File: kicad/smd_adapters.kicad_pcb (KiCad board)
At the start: 2 copper layers, 79.8 x 69.7 mm, 24 parts

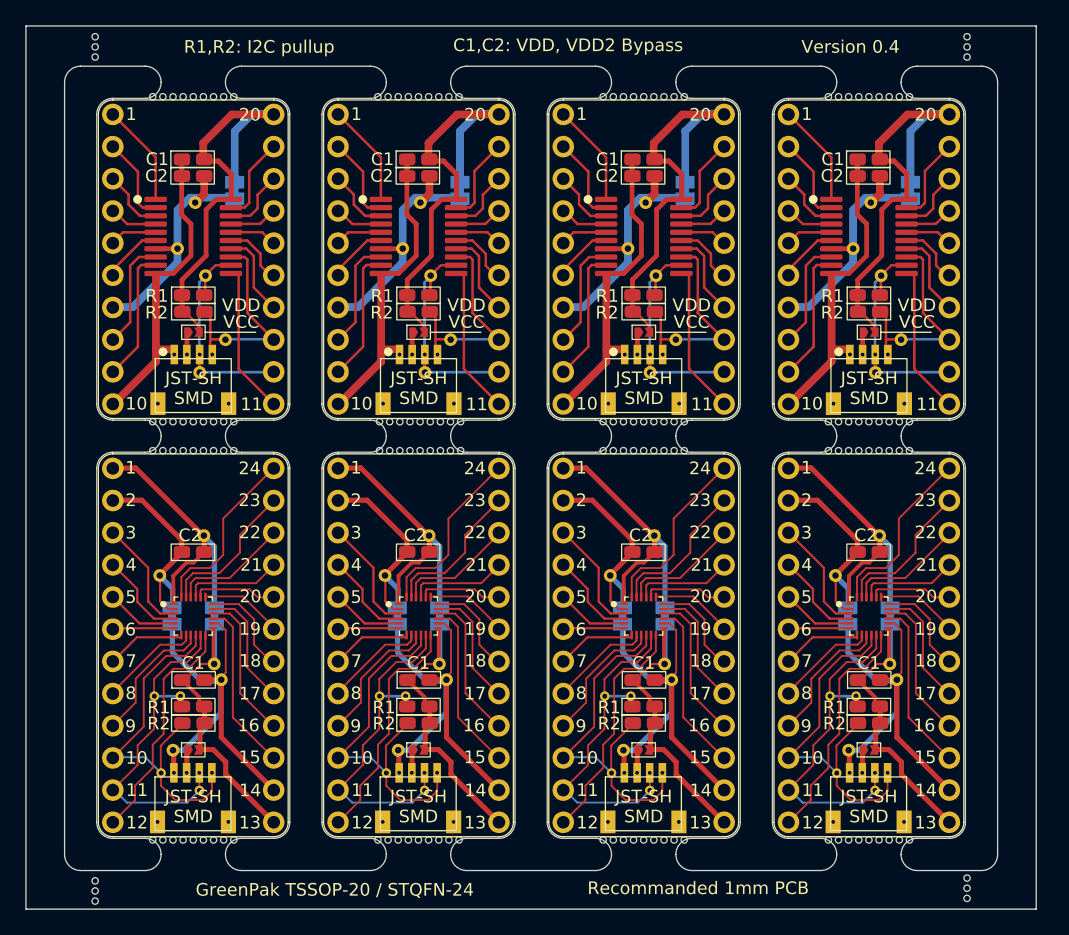
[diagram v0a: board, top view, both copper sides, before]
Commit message: Added the new footprint to the panel.
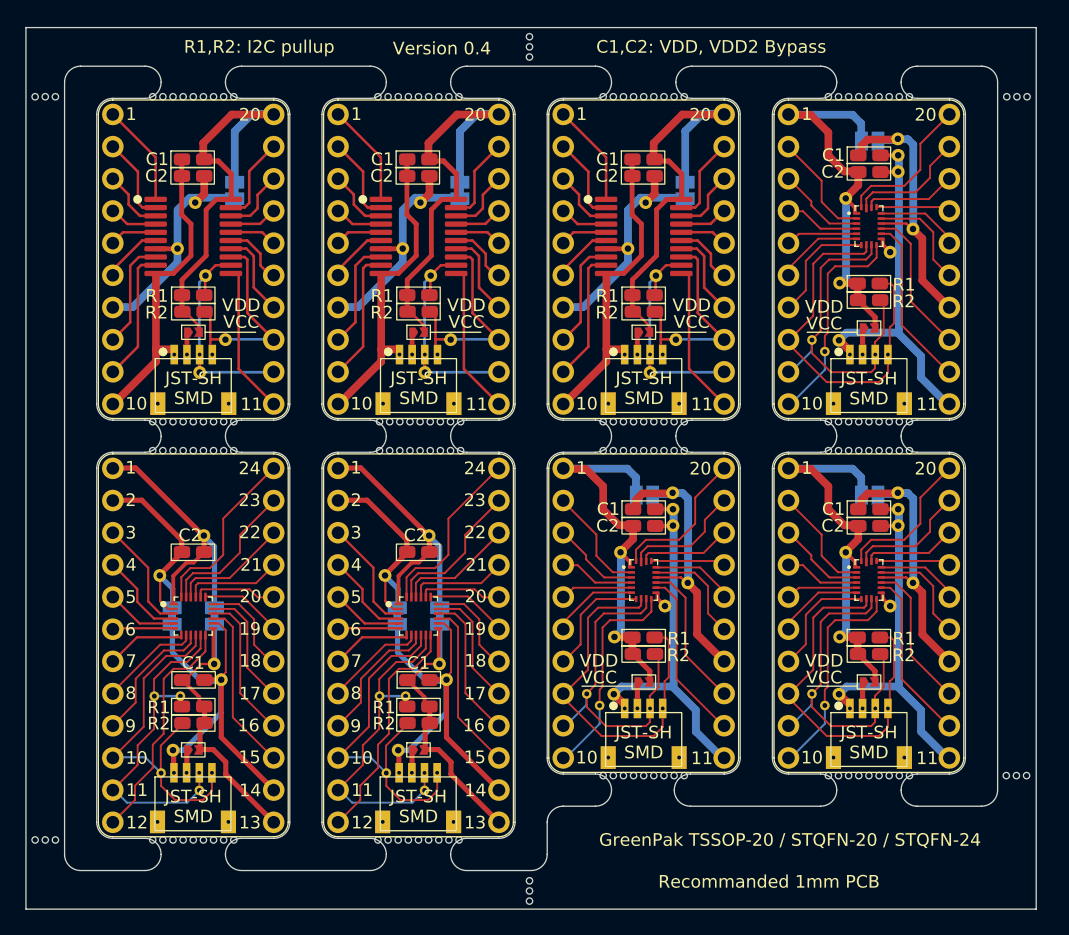
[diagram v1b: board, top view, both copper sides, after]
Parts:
- removed the REF** at (12.2, 9.40)
- removed the REF** at (30.0, -21.1)
- removed the REF** at (30.0, 9.40)
- added REF**: GREENPAK-SMD-ADAPTER-STQFN-20-QWIIC, greenpack_smd_adapters:GREENPAK-SMD-ADAPTER-STQFN-20-QWIIC, F.Cu at (30.0, -21.1)
- added REF**: GREENPAK-SMD-ADAPTER-STQFN-20-QWIIC, greenpack_smd_adapters:GREENPAK-SMD-ADAPTER-STQFN-20-QWIIC, F.Cu at (30.0, 6.86)
- added REF**: GREENPAK-SMD-ADAPTER-STQFN-20-QWIIC, greenpack_smd_adapters:GREENPAK-SMD-ADAPTER-STQFN-20-QWIIC, F.Cu at (12.2, 6.86)
- added mouse-bite-2.54mm-slot: VAL**, greenpack_smd_adapters:mouse-bite-holes-short, F.Cu at (4.32, -37.8)
- added mouse-bite-2.54mm-slot: VAL**, greenpack_smd_adapters:mouse-bite-holes-short, F.Cu at (41.6, 18.5)
- moved mouse-bite-2.54mm-slot 34.5 mm to (4.32, 28.8)
- moved mouse-bite-2.54mm-slot 5.80 mm to (-35.1, -32.8), turned to 180 degrees
- moved mouse-bite-2.54mm-slot 5.08 mm to (30.0, 20.8)
- moved mouse-bite-2.54mm-slot 4.01 mm to (-35.1, 25.9), turned to 180 degrees
- moved mouse-bite-2.54mm-slot 3.95 mm to (41.7, -35.1), turned to 0 degrees
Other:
- board size 79.8 x 69.7 mm -> 79.8 x 69.6 mm
- board text added: "GreenPak TSSOP-20 / STQFN-20 / STQFN-24"
- board text removed: "GreenPak TSSOP-20 / STQFN-24"

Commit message: Generated gerbers.
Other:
- board text added: "Version 0.2"
- board text removed: "Version 0.4"
